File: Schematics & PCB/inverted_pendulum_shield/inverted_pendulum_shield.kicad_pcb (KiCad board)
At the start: 2 copper layers, 0 parts

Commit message: Made initial pcb layout without wiring
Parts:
- added A1: RaspberryPi_Pico, Module:RaspberryPi_Pico_Common_Unspecified, F.Cu at (158.2, 89.7)
- added C1: 100nF, Capacitor_SMD:C_0805_2012Metric, F.Cu at (139.1, 111.0)
- added C10: 2x22uF (47uF), Capacitor_SMD:C_0805_2012Metric, F.Cu at (144.3, 99.8)
- added C2: 47uF, Capacitor_THT:C_Radial_D5.0mm_H11.0mm_P2.00mm, F.Cu at (134.8, 110.2)
- added C3: 100nF, Capacitor_SMD:C_0805_2012Metric, F.Cu at (179.1, 101.9)
- added C4: 100nF, Capacitor_SMD:C_0805_2012Metric, F.Cu at (134.9, 100.1)
- added C5: 10uF, Capacitor_SMD:C_0805_2012Metric, F.Cu at (175.8, 110.2)
- added C6: 47pF, Capacitor_SMD:C_0603_1608Metric, F.Cu at (174.5, 105.9)
- added C7: 2x22uF (47uF), Capacitor_SMD:C_0805_2012Metric, F.Cu at (179.1, 111.0)
- added C8: 10uF, Capacitor_SMD:C_0805_2012Metric, F.Cu at (144.0, 103.4)
- added C9: 12pF, Capacitor_SMD:C_0603_1608Metric, F.Cu at (139.2, 104.4)
- added D1: D_Zener, Diode_SMD:D_SOD-323, F.Cu at (174.4, 92.7)
- added D2: Green, LED_THT:LED_D10.0mm, F.Cu at (174.2, 127.3)
- added D3: Green, LED_THT:LED_D10.0mm, F.Cu at (145.0, 127.3)
- added H1: MountingHole, MountingHole:MountingHole_2.2mm_M2, F.Cu at (124.0, 67.1)
- added H2: MountingHole, MountingHole:MountingHole_2.2mm_M2, F.Cu at (192.0, 67.1)
- added H3: MountingHole, MountingHole:MountingHole_2.2mm_M2, F.Cu at (124.0, 131.1)
- added H4: MountingHole, MountingHole:MountingHole_2.2mm_M2, F.Cu at (192.0, 131.1)
- added J1: Screw_Terminal_01x02, TerminalBlock:TerminalBlock_MaiXu_MX126-5.0-02P_1x02_P5.00mm, F.Cu at (126.0, 77.0)
- added J2: Screw_Terminal_01x02, TerminalBlock:TerminalBlock_MaiXu_MX126-5.0-02P_1x02_P5.00mm, F.Cu at (126.0, 113.6)
- added J3: Screw_Terminal_01x04, TerminalBlock:TerminalBlock_MaiXu_MX126-5.0-04P_1x04_P5.00mm, F.Cu at (126.0, 89.9)
- added J4: FCR7350R, Connector:Banana_Cliff_FCR7350R_S16N-PC_Horizontal, F.Cu at (177.8, 77.5)
- added J5: FCR7350B, Connector:Banana_Cliff_FCR7350B_S16N-PC_Horizontal, F.Cu at (138.7, 77.5)
- added L1: 6.8uH, Inductor_SMD:L_TDK_SLF7045, F.Cu at (184.7, 104.9)
- added L2: 10uH, Inductor_SMD:L_Bourns-SRU1028_10.0x10.0mm, F.Cu at (137.4, 92.7)
- added Q1: FQD8P10TM, Package_TO_SOT_SMD:TO-252-3_TabPin2, F.Cu at (183.0, 90.7)
- added R1: 0.169, Resistor_SMD:R_1206_3216Metric, F.Cu at (133.8, 116.3)
- added R10: 422k, Resistor_SMD:R_0805_2012Metric, F.Cu at (139.2, 106.9)
- added R11: 30.1k, Resistor_SMD:R_0805_2012Metric, F.Cu at (136.1, 103.6)
- added R2: 10k, Resistor_SMD:R_0805_2012Metric, F.Cu at (185.9, 116.5)
- added R3: 1k, Resistor_SMD:R_0805_2012Metric, F.Cu at (160.3, 122.4)
- added R4: 10k, Resistor_SMD:R_0805_2012Metric, F.Cu at (156.2, 122.4)
- added R5: 10k, Resistor_SMD:R_0805_2012Metric, F.Cu at (174.4, 88.9)
- added R6: 1k, Resistor_SMD:R_0805_2012Metric, F.Cu at (164.2, 122.4)
- added R7: 1k, Resistor_SMD:R_0805_2012Metric, F.Cu at (152.2, 122.4)
- added R8: 158k, Resistor_SMD:R_0805_2012Metric, F.Cu at (172.2, 105.9)
- added R9: 30.1k, Resistor_SMD:R_0805_2012Metric, F.Cu at (175.8, 102.6)
- added SW1: 1825027, switches:SW_THT_1825027-G_TEC, F.Cu at (191.8, 118.6)
- added U1: DRV8231DDAR, Package_SO:Texas_HTSOP-8-1EP_3.9x4.9mm_P1.27mm_EP2.95x4.9mm_Mask2.4x3.1mm_ThermalVias, F.Cu at (141.3, 115.5)
- added U2: AP63301WU-7, Package_TO_SOT_SMD:TSOT-23-6, F.Cu at (177.8, 106.9)
- added U3: AP63301WU-7, Package_TO_SOT_SMD:TSOT-23-6, F.Cu at (140.5, 101.0)
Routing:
- added copper zone on B.Cu, net GND
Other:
- board outline added: 76 x 72 mm
- board text added: "Group 22"

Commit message: Finished PCB
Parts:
- H1, H2, H3, H4: footprint MountingHole:MountingHole_2.2mm_M2 -> MountingHole:MountingHole_3.2mm_M3
- moved J3 15.0 mm to (125.0, 104.9), turned to 90 degrees
- moved C3 3.30 mm to (182.4, 101.9)
- moved C6 3.30 mm to (177.8, 105.9)
- moved C7 3.30 mm to (182.4, 111.0)
- moved L1 3.30 mm to (188.0, 104.9)
- moved R8 3.30 mm to (175.5, 105.9)
- moved C5 3.30 mm to (179.1, 110.2)
- moved R9 3.30 mm to (179.1, 102.6)
- moved U2 3.30 mm to (181.1, 106.9)
- moved D2 2.54 mm to (171.7, 127.3), turned to 0 degrees
- moved R11 2.10 mm to (136.1, 101.5)
- moved C4 2.10 mm to (134.9, 98.0)
- moved C10 1.86 mm to (144.5, 98.0)
- moved C8 1.85 mm to (144.0, 101.5)
- moved C9 1.85 mm to (139.2, 102.5)
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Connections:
- A1 pad 10: unconnected-(A1-GPIO7-Pad10)_1 -> IMU_SCL
- A1 pad 20: Controls Start -> unconnected-(A1-GPIO15-Pad20)
- A1 pad 21: unconnected-(A1-GPIO16-Pad21) -> Controls Start
- A1 pad 24: IMU_RST -> unconnected-(A1-GPIO18-Pad24)
- A1 pad 25: IMU_INT -> unconnected-(A1-GPIO19-Pad25)_1
- A1 pad 26: IMU_SDA -> unconnected-(A1-GPIO20-Pad26)
- A1 pad 27: IMU_SCL -> unconnected-(A1-GPIO21-Pad27)
- A1 pad 4: unconnected-(A1-GPIO2-Pad4)_1 -> IMU_RST
- A1 pad 5: unconnected-(A1-GPIO3-Pad5) -> IMU_INT
- A1 pad 9: unconnected-(A1-GPIO6-Pad9)_1 -> IMU_SDA
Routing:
- net +5V: track 0.00 -> 220.2 mm, vias 0 -> 4
- net VDD: track 0.00 -> 127.3 mm
- net Motor Control 1: track 0.00 -> 109.8 mm
- net Motor Control 2: track 0.00 -> 104.0 mm
- net +12V: track 0.00 -> 57.5 mm
- net ADC0: track 0.00 -> 36.5 mm
- net LED_PWM_1: track 0.00 -> 36.0 mm, vias 0 -> 2
- net IMU_SCL: track 0.00 -> 34.7 mm
- net IMU_SDA: track 0.00 -> 31.5 mm
- net IMU_INT: track 0.00 -> 26.9 mm
- net Controls Start: track 0.00 -> 26.6 mm, vias 0 -> 2
- net LED_PWM_2: track 0.00 -> 25.8 mm
- net IMU_RST: track 0.00 -> 25.2 mm
- net GND: track 0.00 -> 24.5 mm, vias 0 -> 25
- net /OUT2: track 0.00 -> 13.5 mm
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- added copper zone on F.Cu, net GND

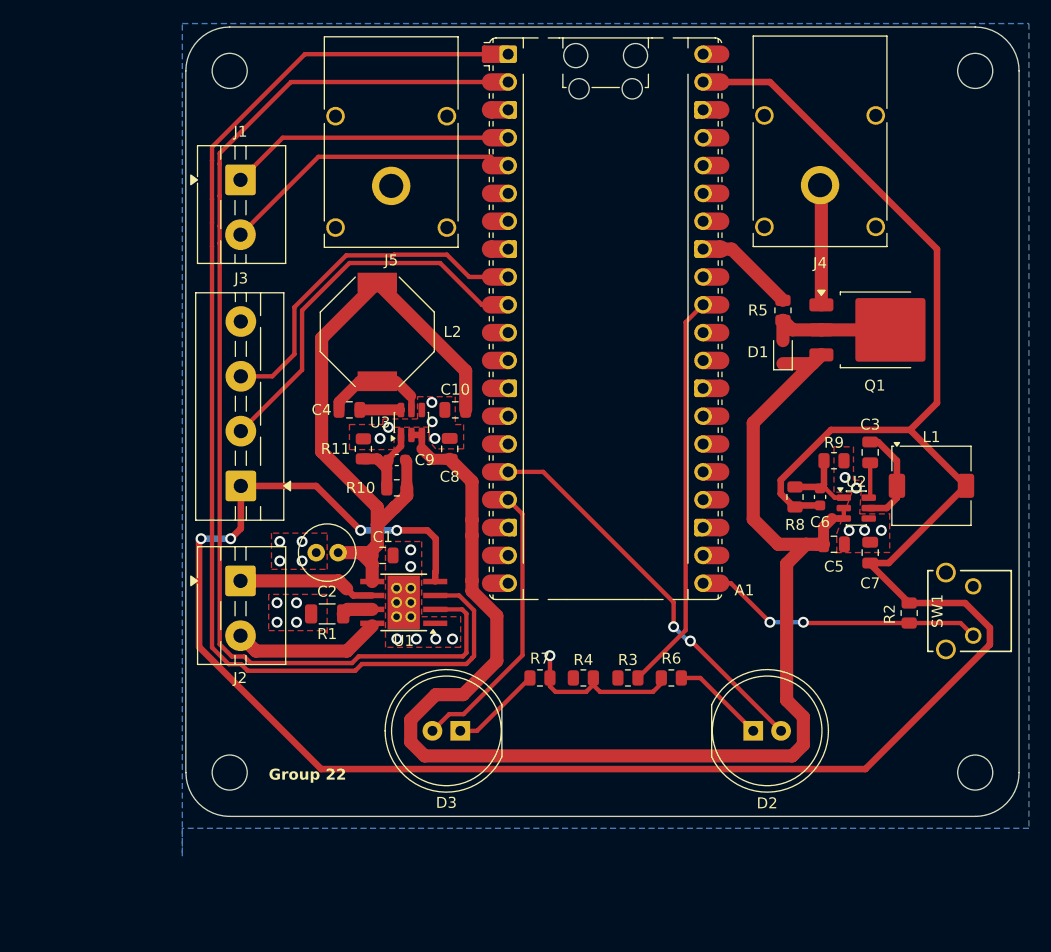
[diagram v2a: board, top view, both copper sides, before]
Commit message: Made next revision of schematic and with parts of pcb done
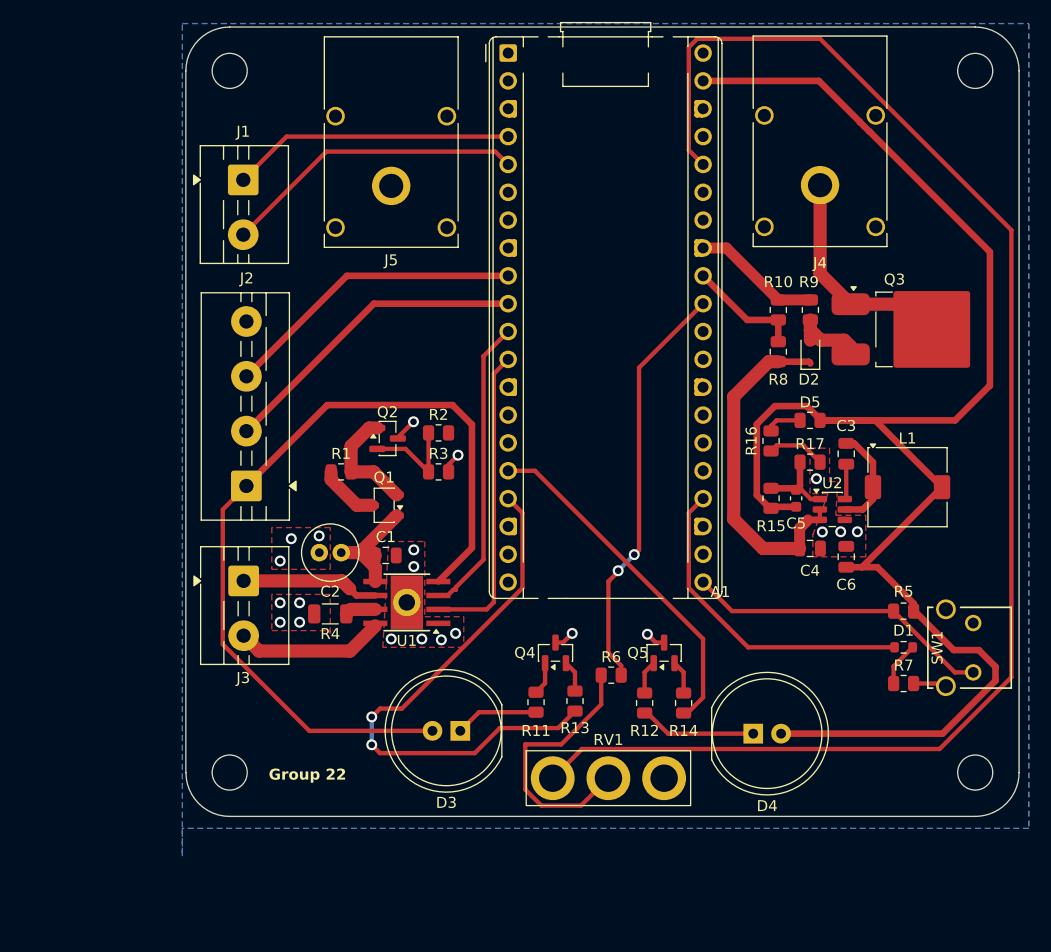
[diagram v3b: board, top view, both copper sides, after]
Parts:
- removed C10: 2x22uF (47uF), Capacitor_SMD:C_0805_2012Metric
- removed the C4 at (134.9, 98.0)
- removed C8: 10uF, Capacitor_SMD:C_0805_2012Metric
- removed C9: 12pF, Capacitor_SMD:C_0603_1608Metric
- removed the D2 at (171.7, 127.3)
- removed L2: 10uH, Inductor_SMD:L_Bourns-SRU1028_10.0x10.0mm
- removed the R11 at (136.1, 101.5)
- removed the R4 at (156.2, 122.4)
- removed the R6 at (164.2, 122.4)
- removed U3: AP63301WU-7, Package_TO_SOT_SMD:TSOT-23-6
- added D1: White, Resistor_SMD:R_0603_1608Metric, F.Cu at (185.4, 119.6)
- added D4: Green, LED_THT:LED_D10.0mm, F.Cu at (171.7, 127.5)
- added D5: Orange, Resistor_SMD:R_0805_2012Metric, F.Cu at (176.9, 98.9)
- added Q1: DMP3056L-7, Package_TO_SOT_SMD:SOT-23-3, F.Cu at (138.0, 106.7)
- added Q2: NX138BKR, Package_TO_SOT_SMD:SOT-23, F.Cu at (138.4, 100.6)
- added Q4: SLMT320V3CN, Package_TO_SOT_SMD:SOT-23, F.Cu at (153.7, 120.1)
- added Q5: SLMT320V3CN, Package_TO_SOT_SMD:SOT-23, F.Cu at (163.6, 120.1)
- added R1: 100k, Resistor_SMD:R_0805_2012Metric, F.Cu at (134.1, 103.6)
- added R12: 180, Resistor_SMD:R_0805_2012Metric, F.Cu at (161.8, 124.7)
- added R13: 180, Resistor_SMD:R_0805_2012Metric, F.Cu at (155.4, 124.5)
- added R14: 180, Resistor_SMD:R_0805_2012Metric, F.Cu at (165.4, 124.7)
- added R16: 2k7, Resistor_SMD:R_0805_2012Metric, F.Cu at (173.3, 100.8)
- added R2: 1k, Resistor_SMD:R_0805_2012Metric, F.Cu at (143.0, 100.1)
- added R3: 10k, Resistor_SMD:R_0805_2012Metric, F.Cu at (143.0, 103.6)
- added R7: 2k7, Resistor_SMD:R_0805_2012Metric, F.Cu at (185.4, 122.9)
- added R8: 82k, Resistor_SMD:R_0805_2012Metric, F.Cu at (174.0, 92.7)
- added RV1: R_Potentiometer, pendulum_footprints:uc_potentiometer, F.Cu at (158.5, 131.6)
- A1: footprint Module:RaspberryPi_Pico_Common_Unspecified -> Module:RaspberryPi_Pico_Common_THT
- C6: renamed from C7; value 2x22uF (47uF) -> 47uF
- Q3: renamed from Q1; footprint Package_TO_SOT_SMD:TO-252-3_TabPin2 -> Package_TO_SOT_SMD:TO-252-2_TabPin1
- R10: value 422k -> 10k
- R11: renamed from R7; value 1k -> 180
- moved R10 38.4 mm to (174.0, 88.9), turned to 90 degrees
- moved A1 25.8 mm to (149.4, 65.4)
- moved SW1 3.35 mm to (191.8, 121.9)
- moved Q3 3.01 mm to (186.0, 90.6)
- moved D2 2.50 mm to (176.9, 92.7)
- moved R9 2.50 mm to (176.9, 88.9)
- moved R11 2.24 mm to (151.9, 124.6), turned to 90 degrees
- moved C6 2.22 mm to (180.2, 111.4)
- moved C4 2.22 mm to (176.9, 110.6)
- moved C3 2.19 mm to (180.2, 102.0)
- moved R17 2.19 mm to (176.9, 102.7)
- moved U2 2.19 mm to (178.9, 107.1)
- moved C5 2.19 mm to (175.6, 106.0)
- moved L1 2.19 mm to (185.8, 105.0)
- moved R15 2.19 mm to (173.3, 106.0)
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- renumbered C5 to C4, C6 to C5, D1 to D2, J3 to J2, J2 to J3, R8 to R15, R9 to R17, R1 to R4, R2 to R5, R3 to R6, R5 to R9
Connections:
- A1 pad 1: Motor Control 1 -> unconnected-(A1-GPIO0-Pad1)
- A1 pad 11: unconnected-(A1-GPIO8-Pad11) -> Motor Control 1
- A1 pad 12: unconnected-(A1-GPIO9-Pad12)_1 -> Motor Control 2
- A1 pad 16: LED_PWM_1 -> LED_PWM_2
- A1 pad 17: LED_PWM_2 -> LED_PWM_1
- A1 pad 2: Motor Control 2 -> unconnected-(A1-GPIO1-Pad2)
- A1 pad 22: unconnected-(A1-GPIO17-Pad22)_1 -> Motor_SW
- A1 pad 24: unconnected-(A1-GPIO18-Pad24) -> /LED_indicate
- A1 pad 32: unconnected-(A1-GPIO27_ADC1-Pad32) -> ADC1
- C1 pad 1: +12V -> Net-(Q1-D)
- C2 pad 1: +12V -> Net-(Q1-D)
- C4 pad 1: VDD -> Vin
- D2 pad 1: VDD -> Vin
- D3 pad 2: LED_PWM_2 -> +5V
- R10 pad 1: +12V -> ADC1
- R10 pad 2: Net-(U3-FB) -> GND
- R11 pad 2: GND -> Net-(Q4-D)
- U1 pad 5: +12V -> Net-(Q1-D)
- U2 pad 2: VDD -> Vin
- U2 pad 3: VDD -> Vin
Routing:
- net +3.3V: track 0.00 -> 134.6 mm
- net VDD: track 127.3 -> 0.00 mm
- net Motor Control 1: track 109.8 -> 27.3 mm
- net Motor Control 2: track 104.0 -> 28.0 mm
- net +12V: track 57.5 -> 0.00 mm
- net Vin: track 0.00 -> 36.7 mm
- net /LED_indicate: track 0.00 -> 29.7 mm
- net Net-(R6-Pad1): track 0.00 -> 24.4 mm
- net LED_PWM_1: track 36.0 -> 50.3 mm
- net Net-(Q1-D): track 0.00 -> 11.0 mm
- net Net-(D4-K): track 0.00 -> 10.7 mm
- net ADC1: track 0.00 -> 10.5 mm
- net Net-(Q1-G): track 0.00 -> 10.4 mm
- net Net-(J4-Pin_1): track 11.0 -> 20.4 mm
- net Net-(Q2-G): track 0.00 -> 9.10 mm
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
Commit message: finished revision 2 of pcb and schematics
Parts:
- moved SW1 80.8 mm to (111.0, 121.8), turned to -90 degrees
- moved R5 72.4 mm to (114.3, 130.1)
- moved R7 71.3 mm to (114.3, 118.0), turned to 180 degrees
- moved D1 69.0 mm to (116.6, 124.1), turned to -90 degrees
- moved J3 51.9 mm to (176.8, 107.8), turned to 90 degrees
- moved Q2 38.9 mm to (169.6, 123.7)
- moved R4 37.6 mm to (168.8, 104.7), turned to 0 degrees
- moved R1 36.7 mm to (167.1, 119.7)
- moved R2 36.2 mm to (174.4, 118.2)
- moved R3 36.2 mm to (174.4, 121.7)
- moved C2 33.7 mm to (167.8, 110.3), turned to 0 degrees
- moved Q1 31.8 mm to (164.8, 123.8)
- moved A1 29.0 mm to (121.2, 72.1)
- moved L1 28.8 mm to (159.3, 116.2)
- moved R16 28.8 mm to (146.9, 112.0)
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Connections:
- A1 pad 11: Motor Control 1 -> unconnected-(A1-GPIO8-Pad11)
- A1 pad 12: Motor Control 2 -> unconnected-(A1-GPIO9-Pad12)
- A1 pad 14: unconnected-(A1-GPIO10-Pad14) -> Controls Start
- A1 pad 15: unconnected-(A1-GPIO11-Pad15) -> /LED_indicate
- A1 pad 21: Controls Start -> unconnected-(A1-GPIO16-Pad21)
- A1 pad 24: /LED_indicate -> unconnected-(A1-GPIO18-Pad24)
- A1 pad 26: unconnected-(A1-GPIO20-Pad26) -> Motor Control 1
- A1 pad 27: unconnected-(A1-GPIO21-Pad27) -> Motor Control 2
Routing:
- net Motor_SW: track 0.00 -> 57.6 mm, vias 0 -> 2
- net +5V: track 221.6 -> 272.5 mm
- net Net-(Q1-D): track 11.0 -> 42.5 mm
- net Vin: track 36.7 -> 55.6 mm
- net Net-(R6-Pad1): track 24.4 -> 8.65 mm
- net IMU_INT: track 27.8 -> 12.3 mm
- net IMU_RST: track 25.8 -> 11.3 mm
- net IMU_SDA: track 27.7 -> 13.2 mm
- net LED_PWM_1: track 50.3 -> 36.1 mm, vias 2 -> 0
- net IMU_SCL: track 28.7 -> 15.5 mm
- net LED_PWM_2: track 31.8 -> 43.8 mm
- net +3.3V: track 134.6 -> 123.0 mm
- net /LED_indicate: track 29.7 -> 19.1 mm
- net ADC0: track 37.9 -> 46.0 mm
- net Motor Control 2: track 28.0 -> 20.1 mm, vias 0 -> 2
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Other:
- board text added: "5V"
- board text added: "Buck Converter"
- board text added: "Controls Feedback"
- board text added: "GND"
- board text added: "H- Bridge"
- board text added: "High-side Switch"
- board text added: "IMU Connections"
- board text added: "INT"
- board text added: "Manual Control"
- board text added: "RST"
- board text added: "RVP"
- board text added: "Reaction Wheel Shield Group 22"
- board text added: "SCL"
- board text added: "SDA"
- board text removed: "Group 22"

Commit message: Meeting changes
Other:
- board text added: "Strain relief holes"

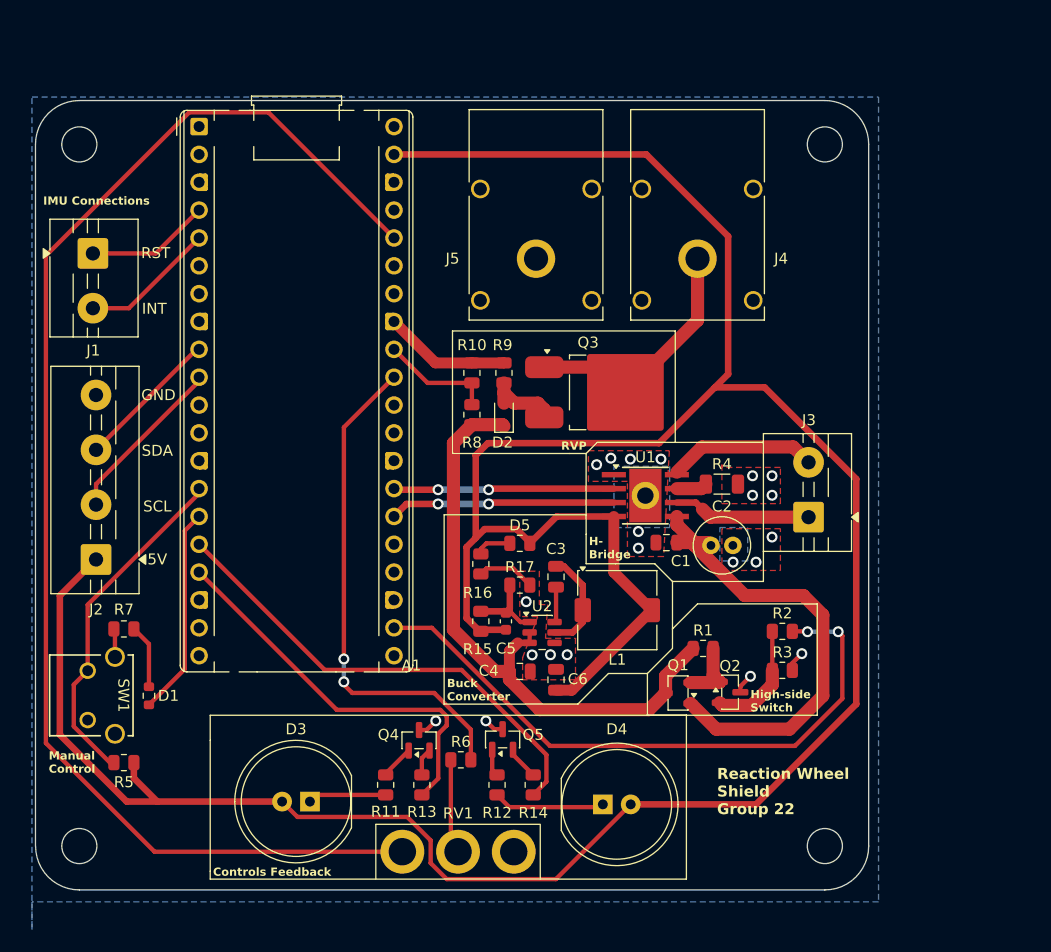
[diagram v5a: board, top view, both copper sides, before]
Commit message: Finished BOM and finalised PCB layout
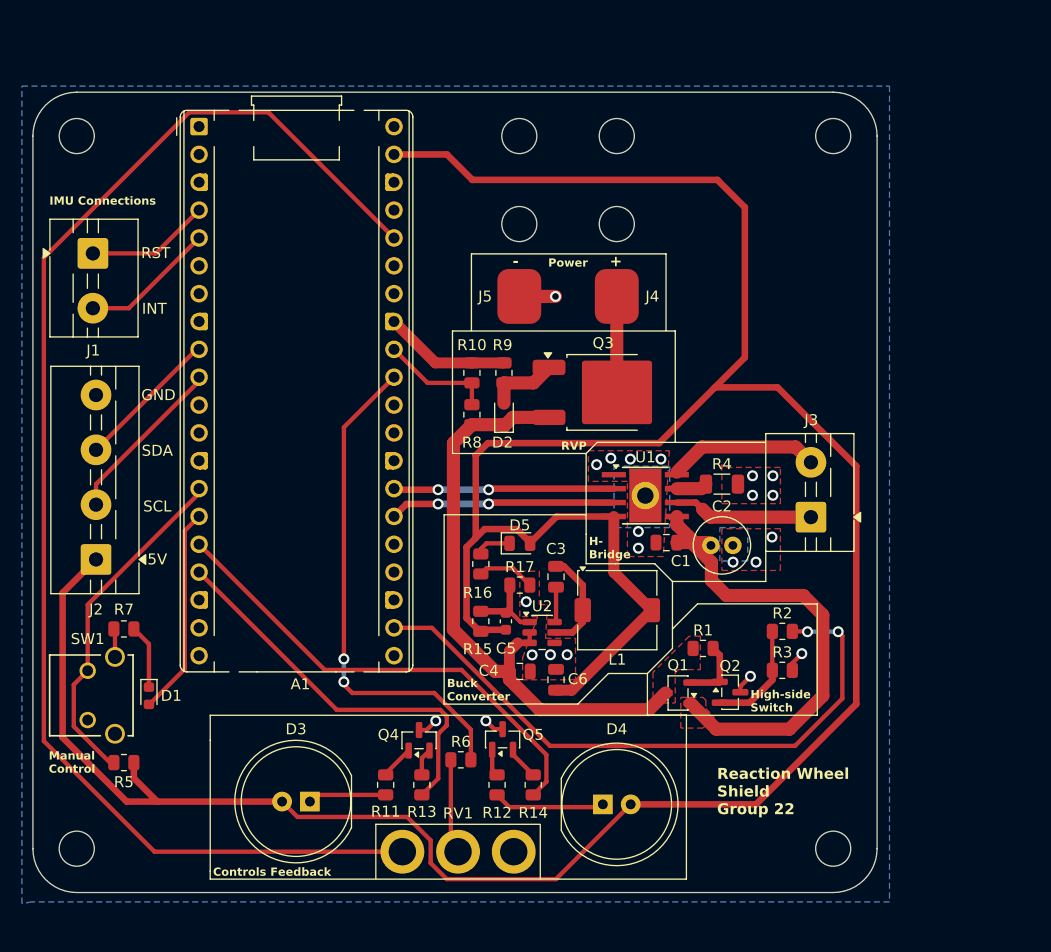
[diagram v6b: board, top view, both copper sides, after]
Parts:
- added H5: MountingHole, MountingHole:MountingHole_3.2mm_M3, F.Cu at (150.4, 81.0)
- added H6: MountingHole, MountingHole:MountingHole_3.2mm_M3, F.Cu at (159.3, 81.0)
- added H7: MountingHole, MountingHole:MountingHole_3.2mm_M3, F.Cu at (159.3, 73.0)
- added H8: MountingHole, MountingHole:MountingHole_3.2mm_M3, F.Cu at (150.4, 73.0)
- D1: footprint Resistor_SMD:R_0603_1608Metric -> LED_SMD:LED_0603_1608Metric
- D5: footprint Resistor_SMD:R_0805_2012Metric -> LED_SMD:LED_0805_2012Metric
- J4: footprint Connector:Banana_Cliff_FCR7350R_S16N-PC_Horizontal -> Connector_Wire:SolderWirePad_1x01_SMD_4x8mm
- J5: footprint Connector:Banana_Cliff_FCR7350B_S16N-PC_Horizontal -> Connector_Wire:SolderWirePad_1x01_SMD_4x8mm
- Q3: footprint Package_TO_SOT_SMD:TO-252-2_TabPin1 -> Package_TO_SOT_SMD:TO-252-2
- moved J4 8.13 mm to (159.3, 87.6), turned to 180 degrees
- moved J5 3.77 mm to (150.4, 87.6), turned to 180 degrees
- moved H2 1.08 mm to (179.0, 73.0)
- moved H4 0.80 mm to (179.0, 138.0)
- moved H1 0.80 mm to (110.0, 73.0)
- moved H3 0.34 mm to (110.0, 138.0)
- moved J3 0.22 mm to (177.0, 107.8)
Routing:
- net Net-(J4-Pin_1): track 23.3 -> 8.76 mm
- net +5V: track 272.5 -> 276.7 mm
- net GND: track 26.9 -> 30.2 mm, vias 21 -> 22
- net Net-(Q1-D): track 42.5 -> 43.5 mm
- net Vin: track 55.6 -> 54.8 mm
- added copper zone on F.Cu, net Net-(Q1-D)
- added copper zone on F.Cu, net Vin
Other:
- board size 76 x 72 mm -> 77 x 73 mm
- board text added: "+"
- board text added: "-"
- board text added: "Hole for better soldering ->"
- board text added: "Power"

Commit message: Finished final schematic and PCB revisions
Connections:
- net Net-(Q1-D) renamed /VM
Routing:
- net /VM: track 43.5 -> 36.4 mm
- net GND: track 30.2 -> 24.3 mm, vias 22 -> 23
- net +3.3V: track 123.1 -> 124.3 mm
- net Controls Start: track 31.5 -> 32.3 mm
